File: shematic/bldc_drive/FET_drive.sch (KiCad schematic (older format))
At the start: 51 parts, among them Q1 BC817, Q2 BC807, Q3 IRF1407, Q4 IRF1407, Q5 IRF1407, Q6 IRF1407, Q7 IRF1407, Q8 IRF1407, Q9 IRF1407, U6 IR2304, U7 IR2304, U8 IR2304, U9 INA193

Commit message: --
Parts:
- R23: footprint Resistor_SMD:R_0805_2012Metric -> Resistor_SMD:R_0603_1608Metric
- U6, U7, U8: footprint Package_SO:SO-8_3.9x4.9mm_P1.27mm -> Package_SO:SOIC-8_3.9x4.9mm_P1.27mm
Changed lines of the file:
@@
 F 0 "U6" H 2650 2450 50  0000 C CNN
 F 1 "IR2304" H 2650 2350 50  0000 C CNN
-F 2 "Package_SO:SO-8_3.9x4.9mm_P1.27mm" H 3050 1950 50  0001 C CIN
+F 2 "Package_SO:SOIC-8_3.9x4.9mm_P1.27mm" H 3050 1950 50  0001 C CIN
 F 3 "https://www.infineon.com/dgdl/ir2304.pdf?fileId=5546d462533600a4015355c9954a16e0" H 3050 1950 50  0001 C CNN
 	1    3050 1950
@@
 F 0 "U7" H 2600 4050 50  0000 C CNN
 F 1 "IR2304" H 2650 3950 50  0000 C CNN
-F 2 "Package_SO:SO-8_3.9x4.9mm_P1.27mm" H 3050 3650 50  0001 C CIN
+F 2 "Package_SO:SOIC-8_3.9x4.9mm_P1.27mm" H 3050 3650 50  0001 C CIN
 F 3 "https://www.infineon.com/dgdl/ir2304.pdf?fileId=5546d462533600a4015355c9954a16e0" H 3050 3650 50  0001 C CNN
 	1    3050 3650
@@
 F 0 "U8" H 2650 5700 50  0000 C CNN
 F 1 "IR2304" H 2650 5600 50  0000 C CNN
-F 2 "Package_SO:SO-8_3.9x4.9mm_P1.27mm" H 3050 5200 50  0001 C CIN
+F 2 "Package_SO:SOIC-8_3.9x4.9mm_P1.27mm" H 3050 5200 50  0001 C CIN
 F 3 "https://www.infineon.com/dgdl/ir2304.pdf?fileId=5546d462533600a4015355c9954a16e0" H 3050 5200 50  0001 C CNN
 	1    3050 5200
@@
 F 0 "R23" V 6143 1750 50  0000 C CNN
 F 1 "1k" V 6234 1750 50  0000 C CNN
-F 2 "Resistor_SMD:R_0805_2012Metric" V 6280 1750 50  0001 C CNN
+F 2 "Resistor_SMD:R_0603_1608Metric" V 6280 1750 50  0001 C CNN
 F 3 "~" H 6350 1750 50  0001 C CNN
 	1    6350 1750

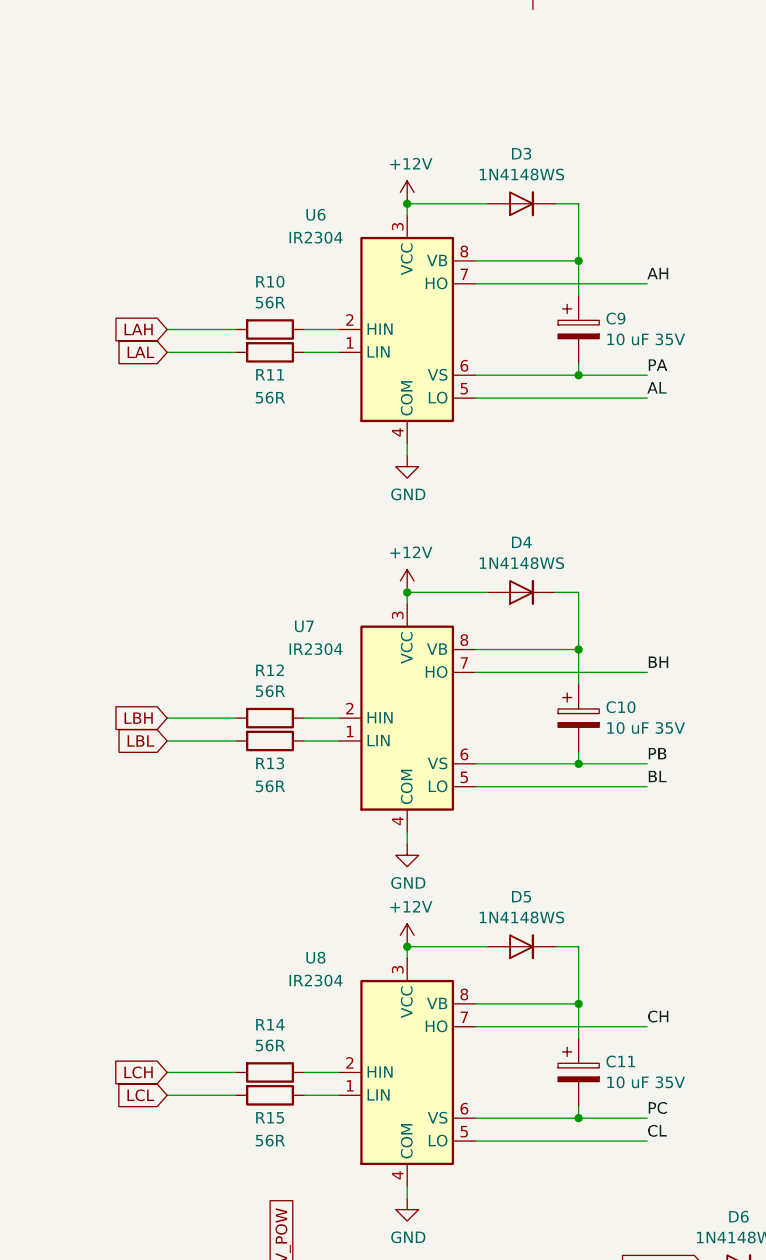
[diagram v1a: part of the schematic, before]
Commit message: replace ir2304 to ir2101
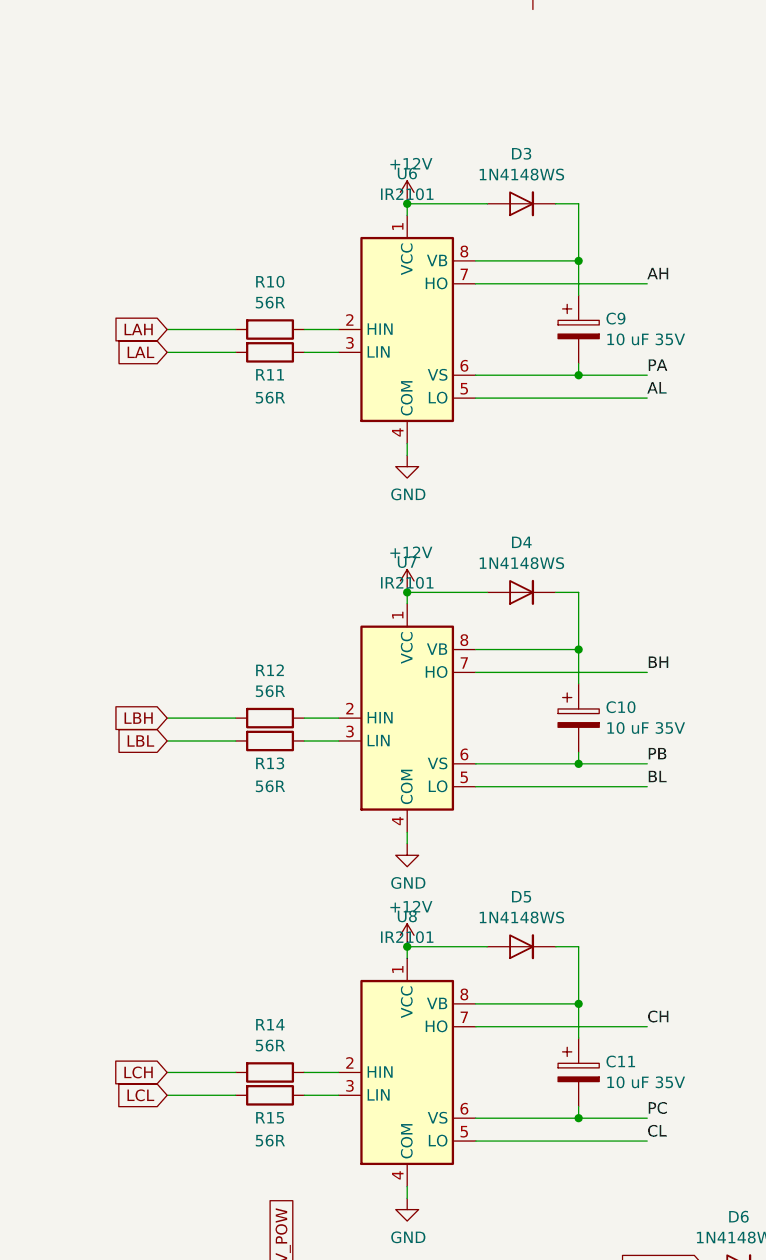
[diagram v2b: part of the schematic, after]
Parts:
- removed U6, U7, U8: IR2304, Package_SO:SOIC-8_3.9x4.9mm_P1.27mm, symbol Driver_FET:IR2304
- added U6, U7, U8: IR2101, Package_SO:SOIC-8_3.9x4.9mm_P1.27mm, symbol Driver_FET:IR2101
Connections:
- net +12V: now also U6.1 (VCC), U7.1 (VCC), U8.1 (VCC)
- net AH: now also U6.7 (HO)
- net AL: now also U6.5 (LO)
- net BH: now also U7.7 (HO)
- net BL: now also U7.5 (LO)
- net CH: now also U8.7 (HO)
- net CL: now also U8.5 (LO)
- net GND: now also U6.4 (COM), U7.4 (COM), U8.4 (COM)
- net PA: now also U6.6 (VS)
- net PB: now also U7.6 (VS)
- net PC: now also U8.6 (VS)
- net at R11.1: now also U6.3 (LIN)
- net at R10.1: now also U6.2 (HIN)
- net at C9.1, D3.1 (K): now also U6.8 (VB)
- net at R13.1: now also U7.3 (LIN)
- net at R12.1: now also U7.2 (HIN)
- net at C10.1, D4.1 (K): now also U7.8 (VB)
- net at R15.1: now also U8.3 (LIN)
- net at R14.1: now also U8.2 (HIN)
- net at C11.1, D5.1 (K): now also U8.8 (VB)
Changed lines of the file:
@@
 $EndDescr
-$Comp
-L Driver_FET:IR2304 U?
-U 1 1 5EACF915
-P 3050 1950
-AR Path="/5EAC8274/5EACF915" Ref="U?"  Part="1"
-AR Path="/5EACE430/5EACF915" Ref="U6"  Part="1"
-F 0 "U6" H 2650 2450 50  0000 C CNN
-F 1 "IR2304" H 2650 2350 50  0000 C CNN
-F 2 "Package_SO:SOIC-8_3.9x4.9mm_P1.27mm" H 3050 1950 50  0001 C CIN
-F 3 "https://www.infineon.com/dgdl/ir2304.pdf?fileId=5546d462533600a4015355c9954a16e0" H 3050 1950 50  0001 C CNN
-	1    3050 1950
-	1    0    0    -1
-$EndComp
-$Comp
-L Driver_FET:IR2304 U?
-U 1 1 5EACF91B
-P 3050 3650
-AR Path="/5EAC8274/5EACF91B" Ref="U?"  Part="1"
-AR Path="/5EACE430/5EACF91B" Ref="U7"  Part="1"
-F 0 "U7" H 2600 4050 50  0000 C CNN
-F 1 "IR2304" H 2650 3950 50  0000 C CNN
-F 2 "Package_SO:SOIC-8_3.9x4.9mm_P1.27mm" H 3050 3650 50  0001 C CIN
-F 3 "https://www.infineon.com/dgdl/ir2304.pdf?fileId=5546d462533600a4015355c9954a16e0" H 3050 3650 50  0001 C CNN
-	1    3050 3650
-	1    0    0    -1
-$EndComp
-$Comp
-L Driver_FET:IR2304 U?
-U 1 1 5EACF921
-P 3050 5200
-AR Path="/5EAC8274/5EACF921" Ref="U?"  Part="1"
-AR Path="/5EACE430/5EACF921" Ref="U8"  Part="1"
-F 0 "U8" H 2650 5700 50  0000 C CNN
-F 1 "IR2304" H 2650 5600 50  0000 C CNN
-F 2 "Package_SO:SOIC-8_3.9x4.9mm_P1.27mm" H 3050 5200 50  0001 C CIN
-F 3 "https://www.infineon.com/dgdl/ir2304.pdf?fileId=5546d462533600a4015355c9954a16e0" H 3050 5200 50  0001 C CNN
-	1    3050 5200
-	1    0    0    -1
-$EndComp
 $Comp
 L power:GND #PWR032
@@
 Wire Wire Line
 	6500 4100 6500 4350
+$Comp
+L Driver_FET:IR2101 U6
+U 1 1 5F508908
+P 3050 1950
+F 0 "U6" H 3050 2631 50  0000 C CNN
+F 1 "IR2101" H 3050 2540 50  0000 C CNN
+F 2 "Package_SO:SOIC-8_3.9x4.9mm_P1.27mm" H 3050 1950 50  0001 C CIN
+F 3 "https://www.infineon.com/dgdl/ir2101.pdf?fileId=5546d462533600a4015355c7a755166c" H 3050 1950 50  0001 C CNN
+	1    3050 1950
+	1    0    0    -1
+$EndComp
+$Comp
+L Driver_FET:IR2101 U7
+U 1 1 5F50A091
+P 3050 3650
+F 0 "U7" H 3050 4331 50  0000 C CNN
+F 1 "IR2101" H 3050 4240 50  0000 C CNN
+F 2 "Package_SO:SOIC-8_3.9x4.9mm_P1.27mm" H 3050 3650 50  0001 C CIN
+F 3 "https://www.infineon.com/dgdl/ir2101.pdf?fileId=5546d462533600a4015355c7a755166c" H 3050 3650 50  0001 C CNN
+	1    3050 3650
+	1    0    0    -1
+$EndComp
+$Comp
+L Driver_FET:IR2101 U8
+U 1 1 5F50ABDC
+P 3050 5200
+F 0 "U8" H 3050 5881 50  0000 C CNN
+F 1 "IR2101" H 3050 5790 50  0000 C CNN
+F 2 "Package_SO:SOIC-8_3.9x4.9mm_P1.27mm" H 3050 5200 50  0001 C CIN
+F 3 "https://www.infineon.com/dgdl/ir2101.pdf?fileId=5546d462533600a4015355c7a755166c" H 3050 5200 50  0001 C CNN
+	1    3050 5200
+	1    0    0    -1
+$EndComp
 $EndSCHEMATC

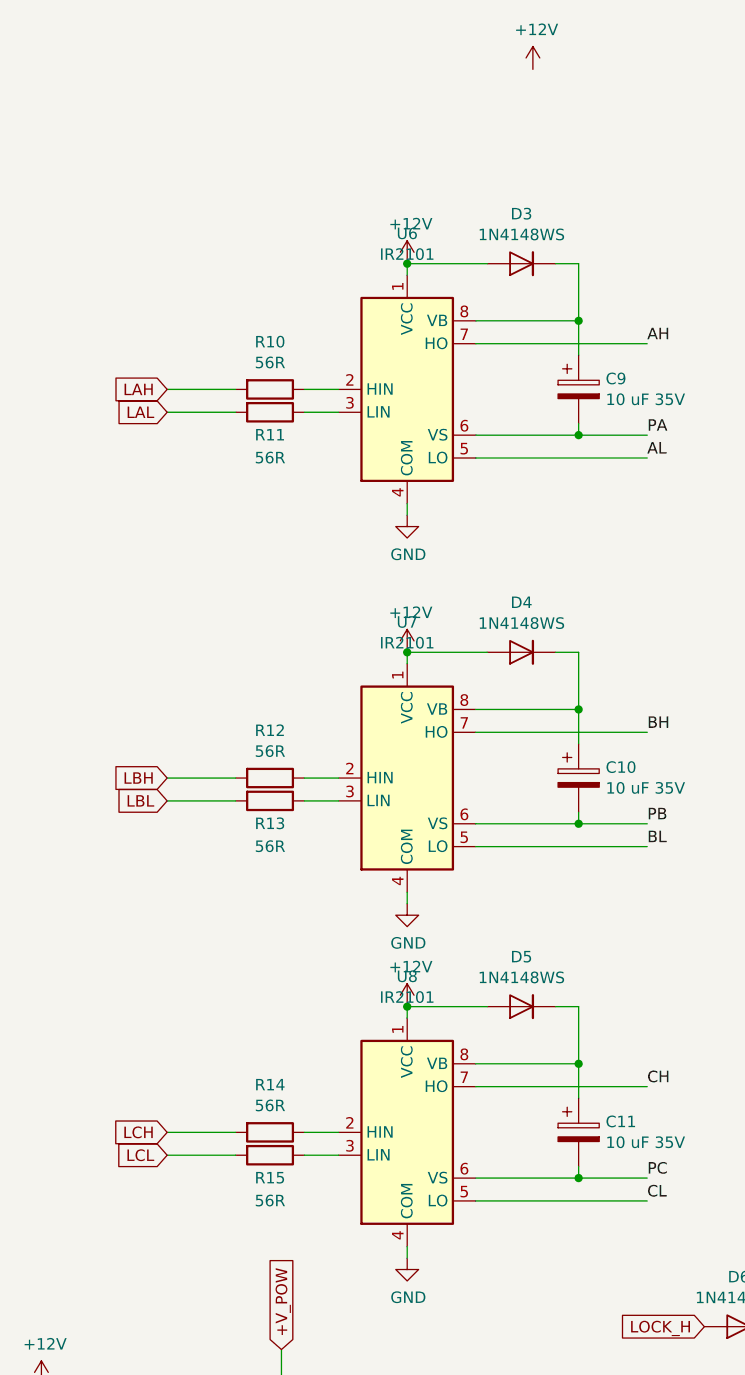
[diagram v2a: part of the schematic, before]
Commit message: modify for warios drive
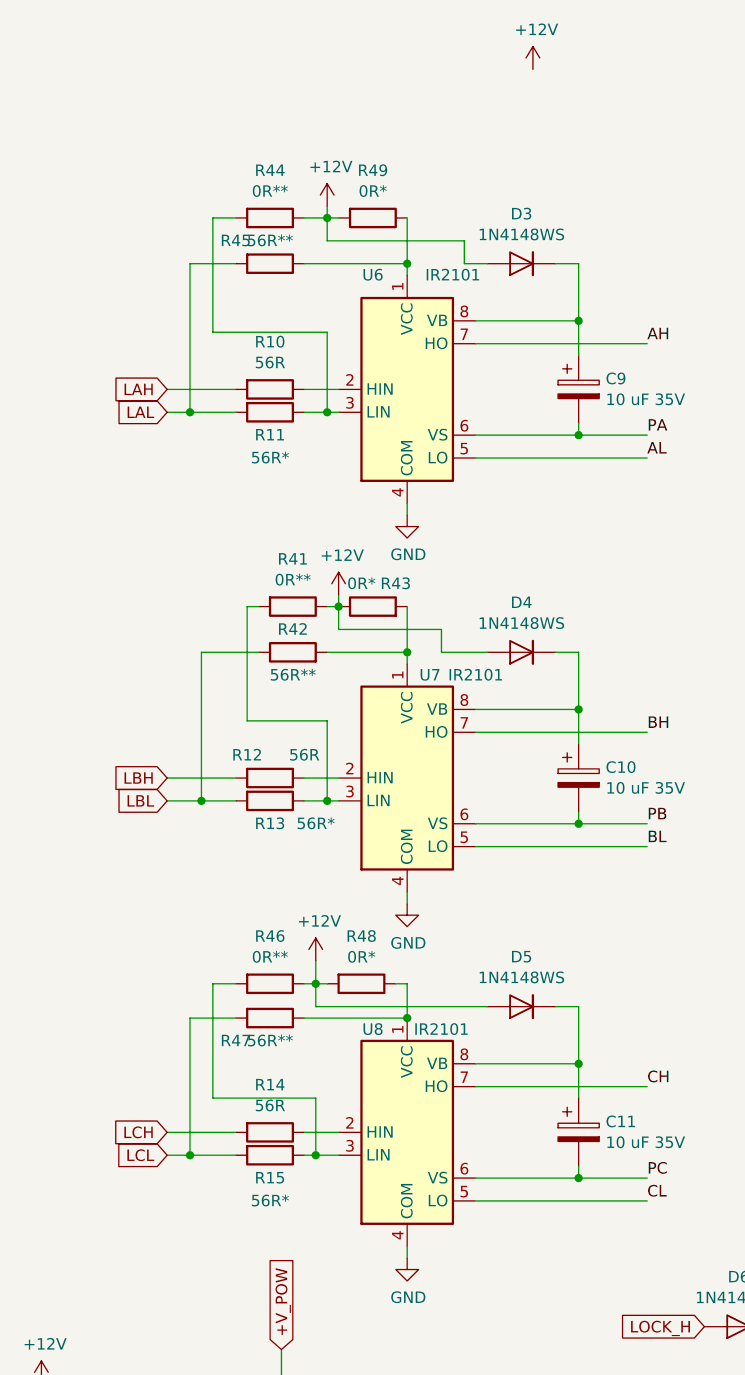
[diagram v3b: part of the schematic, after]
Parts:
- added R41, R44, R46: 0R**, Resistor_SMD:R_0603_1608Metric, symbol Device:R
- added R42, R45, R47: 56R**, Resistor_SMD:R_0603_1608Metric, symbol Device:R
- added R43, R48, R49: 0R*, Resistor_SMD:R_0603_1608Metric, symbol Device:R
- R11, R13, R15: value 56R -> 56R*
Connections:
- net +12V: now also R41.1, R43.1, R44.1, R46.1, R48.2, R49.2; no longer U6.1 (VCC), U7.1 (VCC), U8.1 (VCC)
- net LAL: now also R45.2
- net LBL: now also R42.1
- net LCL: now also R47.2
- net at R11.1, U6.3 (LIN): now also R44.2
- net at R13.1, U7.3 (LIN): now also R41.2
- net at R15.1, U8.3 (LIN): now also R46.2
- new net: R45.1, R49.1, U6.1 (VCC)
- new net: R42.2, R43.2, U7.1 (VCC)
- new net: R47.1, R48.1, U8.1 (VCC)
